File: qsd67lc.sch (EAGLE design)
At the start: 43 parts, among them IC1 MEGA8-P, IC2 BTS555E3146, IC3 MAX3232CPE, IC4 LM2576S, T1 BCR141, U1 HC_05, X2 RS232

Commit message: added connectors fixed rs232 dsub9 pinning added current supply circuit
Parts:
- added R10, R11, R13: 10k, rcl:R-EU_R0805
- added X1: FFKV3, con-phoenix-508:FFKV3
- added X3, X4: FFKV4, con-phoenix-508:FFKV4
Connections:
- removed net IGN_OUT: IC2.O1, IC2.O2
- new net 12V_OUT: IC2.O1, IC2.O2, X4-4.2
- new net IGN0_IN: R13.2, X3-1.2
- new net IGN0_OUT: X4-1.2
- new net IGN1_IN: X3-2.2
- new net IGN1_OUT: X4-2.2
- new net IGN2_IN: X3-3.2
- new net IGN2_OUT: X4-3.2
- new net QS+: IC1.PD2(INT0), R10.1, X1-2.2
- new net QS-: X1-1.2
- net +12V: now also X3-4.2
- net +3V3: now also R10.2
- net GND: now also R11.1, X1-3.2
- net RPM_INT: now also R11.2, R13.1
- net RS232_RX: now also X2.3; no longer X2.2
- net RS232_TX: now also X2.2; no longer X2.3

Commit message: added correct connector devices
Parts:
- removed X1: FFKV3, con-phoenix-508:FFKV3
- removed X3, X4: FFKV4, con-phoenix-508:FFKV4
- added CON1, CON2: RIA-AKL-230-04, con-ria:RIA-AKL-230-04
- added CON3: RIA-AKL-230-03, con-ria:RIA-AKL-230-03
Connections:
- removed net IGN1_IN: X3-2.2
- new net ING1_IN: CON1.P$2
- net +12V: now also CON1.P$4; no longer X3-4.2
- net 12V_OUT: now also CON2.P$4; no longer X4-4.2
- net GND: now also CON3.P$1; no longer X1-3.2
- net IGN0_IN: now also CON1.P$3; no longer X3-1.2
- net IGN0_OUT: now also CON2.P$3; no longer X4-1.2
- net IGN1_OUT: now also CON2.P$2; no longer X4-2.2
- net IGN2_IN: now also CON1.P$1; no longer X3-3.2
- net IGN2_OUT: now also CON2.P$1; no longer X4-3.2
- net QS+: now also CON3.P$3; no longer X1-2.2
- net QS-: now also CON3.P$2; no longer X1-1.2
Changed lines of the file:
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@@
 <part name="+3V6" library="supply1" library_urn="urn:adsk.eagle:library:371" deviceset="+3V3" device=""/>
 <part name="R10" library="rcl" library_urn="urn:adsk.eagle:library:334" deviceset="R-EU_" device="R0805" package3d_urn="urn:adsk.eagle:package:23553/2" value="10k"/>
-<part name="X1" library="con-phoenix-508" library_urn="urn:adsk.eagle:library:176" deviceset="FFKV3" device="" package3d_urn="urn:adsk.eagle:package:9576/1"/>
-<part name="X3" library="con-phoenix-508" library_urn="urn:adsk.eagle:library:176" deviceset="FFKV4" device="" package3d_urn="urn:adsk.eagle:package:9586/1"/>
-<part name="X4" library="con-phoenix-508" library_urn="urn:adsk.eagle:library:176" deviceset="FFKV4" device="" package3d_urn="urn:adsk.eagle:package:9586/1"/>
 <part name="R11" library="rcl" library_urn="urn:adsk.eagle:library:334" deviceset="R-EU_" device="R0805" package3d_urn="urn:adsk.eagle:package:23553/2" value="10k"/>
 <part name="R13" library="rcl" library_urn="urn:adsk.eagle:library:334" deviceset="R-EU_" device="R0805" package3d_urn="urn:adsk.eagle:package:23553/2" value="10k"/>
 <part name="GND9" library="supply1" library_urn="urn:adsk.eagle:library:371" deviceset="GND" device=""/>
+<part name="CON1" library="con-ria" deviceset="RIA-AKL-230-04" device=""/>
+<part name="CON2" library="con-ria" deviceset="RIA-AKL-230-04" device=""/>
+<part name="CON3" library="con-ria" deviceset="RIA-AKL-230-03" device=""/>
+<part name="GND17" library="supply1" library_urn="urn:adsk.eagle:library:371" deviceset="GND" device=""/>
+<part name="P+4" library="supply1" library_urn="urn:adsk.eagle:library:371" deviceset="+12V" device=""/>
 </parts>
 <sheets>
@@
 </plain>
 <instances>
-<instance part="X1" gate="-1" x="-7.62" y="-35.56" rot="R180">
-<attribute name="NAME" x="-7.366" y="-36.449" size="1.778" layer="95"/>
-</instance>
-<instance part="X1" gate="-2" x="-7.62" y="-30.48" rot="R180">
-<attribute name="NAME" x="-7.366" y="-31.369" size="1.778" layer="95"/>
-<attribute name="VALUE" x="-5.08" y="-26.797" size="1.778" layer="96" rot="R180"/>
-</instance>
-<instance part="X3" gate="-1" x="-7.62" y="-12.7" rot="R180">
-<attribute name="NAME" x="-7.366" y="-13.589" size="1.778" layer="95"/>
-</instance>
-<instance part="X3" gate="-2" x="-7.62" y="-7.62" rot="R180">
-<attribute name="NAME" x="-7.366" y="-8.509" size="1.778" layer="95"/>
-</instance>
-<instance part="X3" gate="-3" x="-7.62" y="-2.54" rot="R180">
-<attribute name="NAME" x="-7.366" y="-3.429" size="1.778" layer="95"/>
-</instance>
-<instance part="X3" gate="-4" x="-7.62" y="2.54" rot="R180">
-<attribute name="NAME" x="-7.366" y="1.651" size="1.778" layer="95"/>
-<attribute name="VALUE" x="-5.08" y="6.223" size="1.778" layer="96" rot="R180"/>
-</instance>
-<instance part="X4" gate="-1" x="-7.62" y="12.7" rot="R180">
-<attribute name="NAME" x="-7.366" y="11.811" size="1.778" layer="95"/>
-</instance>
-<instance part="X4" gate="-2" x="-7.62" y="17.78" rot="R180">
-<attribute name="NAME" x="-7.366" y="16.891" size="1.778" layer="95"/>
-</instance>
-<instance part="X4" gate="-3" x="-7.62" y="22.86" rot="R180">
-<attribute name="NAME" x="-7.366" y="21.971" size="1.778" layer="95"/>
-</instance>
-<instance part="X4" gate="-4" x="-7.62" y="27.94" rot="R180">
-<attribute name="NAME" x="-7.366" y="27.051" size="1.778" layer="95"/>
-<attribute name="VALUE" x="-5.08" y="31.623" size="1.778" layer="96" rot="R180"/>
-</instance>
-<instance part="X1" gate="-3" x="-7.62" y="-25.4" rot="R180">
-<attribute name="NAME" x="-7.366" y="-26.289" size="1.778" layer="95"/>
-<attribute name="VALUE" x="-5.08" y="-21.717" size="1.778" layer="96" rot="R180"/>
+<instance part="CON1" gate="G$1" x="7.62" y="17.78" rot="R180"/>
+<instance part="CON2" gate="G$1" x="7.62" y="-5.08" rot="R180"/>
+<instance part="CON3" gate="G$1" x="7.62" y="-30.48" rot="R180"/>
+<instance part="GND17" gate="1" x="-33.02" y="-38.1">
+<attribute name="VALUE" x="-35.56" y="-40.64" size="1.778" layer="96"/>
+</instance>
+<instance part="P+4" gate="1" x="-33.02" y="25.4">
+<attribute name="VALUE" x="-35.56" y="20.32" size="1.778" layer="96" rot="R90"/>
 </instance>
 </instances>
@@
 </busses>
 <nets>
+<net name="+12V" class="0">
+<segment>
+<pinref part="CON1" gate="G$1" pin="P$4"/>
+<wire x1="-5.08" y1="20.32" x2="-33.02" y2="20.32" width="0.1524" layer="91"/>
+<pinref part="P+4" gate="1" pin="+12V"/>
+<wire x1="-33.02" y1="20.32" x2="-33.02" y2="22.86" width="0.1524" layer="91"/>
+</segment>
+</net>
+<net name="IGN0_IN" class="0">
+<segment>
+<pinref part="CON1" gate="G$1" pin="P$3"/>
+<wire x1="-5.08" y1="17.78" x2="-30.48" y2="17.78" width="0.1524" layer="91"/>
+<label x="-30.48" y="17.78" size="1.778" layer="95"/>
+</segment>
+</net>
+<net name="ING1_IN" class="0">
+<segment>
+<pinref part="CON1" gate="G$1" pin="P$2"/>
+<wire x1="-5.08" y1="15.24" x2="-30.48" y2="15.24" width="0.1524" layer="91"/>
+<label x="-30.48" y="15.24" size="1.778" layer="95"/>
+</segment>
+</net>
+<net name="IGN2_IN" class="0">
+<segment>
+<pinref part="CON1" gate="G$1" pin="P$1"/>
+<wire x1="-5.08" y1="12.7" x2="-30.48" y2="12.7" width="0.1524" layer="91"/>
+<label x="-30.48" y="12.7" size="1.778" layer="95"/>
+</segment>
+</net>
+<net name="12V_OUT" class="0">
+<segment>
+<pinref part="CON2" gate="G$1" pin="P$4"/>
+<wire x1="-5.08" y1="-2.54" x2="-30.48" y2="-2.54" width="0.1524" layer="91"/>
+<label x="-30.48" y="-2.54" size="1.778" layer="95"/>
+</segment>
+</net>
+<net name="IGN0_OUT" class="0">
+<segment>
+<pinref part="CON2" gate="G$1" pin="P$3"/>
+<wire x1="-5.08" y1="-5.08" x2="-30.48" y2="-5.08" width="0.1524" layer="91"/>
+<label x="-30.48" y="-5.08" size="1.778" layer="95"/>
+</segment>
+</net>
+<net name="IGN1_OUT" class="0">
+<segment>
+<pinref part="CON2" gate="G$1" pin="P$2"/>
+<wire x1="-5.08" y1="-7.62" x2="-30.48" y2="-7.62" width="0.1524" layer="91"/>
+<label x="-30.48" y="-7.62" size="1.778" layer="95"/>
+</segment>
+</net>
+<net name="IGN2_OUT" class="0">
+<segment>
+<pinref part="CON2" gate="G$1" pin="P$1"/>
+<wire x1="-5.08" y1="-10.16" x2="-30.48" y2="-10.16" width="0.1524" layer="91"/>
+<label x="-30.48" y="-10.16" size="1.778" layer="95"/>
+</segment>
+</net>
 <net name="QS+" class="0">
 <segment>
-<pinref part="X1" gate="-2" pin="2"/>
-<wire x1="-15.24" y1="-30.48" x2="-45.72" y2="-30.48" width="0.1524" layer="91"/>
-<label x="-45.72" y="-30.48" size="1.778" layer="95"/>
+<pinref part="CON3" gate="G$1" pin="P$3"/>
+<wire x1="-5.08" y1="-27.94" x2="-30.48" y2="-27.94" width="0.1524" layer="91"/>
+<label x="-30.48" y="-27.94" size="1.778" layer="95"/>
 </segment>
 </net>
 <net name="QS-" class="0">
 <segment>
-<pinref part="X1" gate="-1" pin="2"/>
-<wire x1="-15.24" y1="-35.56" x2="-45.72" y2="-35.56" width="0.1524" layer="91"/>
-<label x="-45.72" y="-35.56" size="1.778" layer="95"/>
-</segment>
-</net>
-<net name="12V_OUT" class="0">
-<segment>
-<pinref part="X4" gate="-4" pin="2"/>
-<wire x1="-15.24" y1="27.94" x2="-45.72" y2="27.94" width="0.1524" layer="91"/>
-<label x="-45.72" y="27.94" size="1.778" layer="95"/>
-</segment>
-</net>
-<net name="IGN2_OUT" class="0">
-<segment>
-<pinref part="X4" gate="-3" pin="2"/>
-<wire x1="-15.24" y1="22.86" x2="-45.72" y2="22.86" width="0.1524" layer="91"/>
-<label x="-45.72" y="22.86" size="1.778" layer="95"/>
-</segment>
-</net>
-<net name="IGN1_OUT" class="0">
-<segment>
-<pinref part="X4" gate="-2" pin="2"/>
-<wire x1="-15.24" y1="17.78" x2="-45.72" y2="17.78" width="0.1524" layer="91"/>
-<label x="-45.72" y="17.78" size="1.778" layer="95"/>
-</segment>
-</net>
-<net name="IGN0_OUT" class="0">
-<segment>
-<pinref part="X4" gate="-1" pin="2"/>
-<wire x1="-15.24" y1="12.7" x2="-45.72" y2="12.7" width="0.1524" layer="91"/>
-<label x="-45.72" y="12.7" size="1.778" layer="95"/>
-</segment>
-</net>
-<net name="+12V" class="0">
-<segment>
-<pinref part="X3" gate="-4" pin="2"/>
-<wire x1="-15.24" y1="2.54" x2="-45.72" y2="2.54" width="0.1524" layer="91"/>
-<label x="-45.72" y="2.54" size="1.778" layer="95"/>
-</segment>
-</net>
-<net name="IGN2_IN" class="0">
-<segment>
-<pinref part="X3" gate="-3" pin="2"/>
-<wire x1="-15.24" y1="-2.54" x2="-45.72" y2="-2.54" width="0.1524" layer="91"/>
-<label x="-45.72" y="-2.54" size="1.778" layer="95"/>
-</segment>
-</net>
-<net name="IGN1_IN" class="0">
-<segment>
-<pinref part="X3" gate="-2" pin="2"/>
-<wire x1="-15.24" y1="-7.62" x2="-45.72" y2="-7.62" width="0.1524" layer="91"/>
-<label x="-45.72" y="-7.62" size="1.778" layer="95"/>
-</segment>
-</net>
-<net name="IGN0_IN" class="0">
-<segment>
-<pinref part="X3" gate="-1" pin="2"/>
-<wire x1="-15.24" y1="-12.7" x2="-45.72" y2="-12.7" width="0.1524" layer="91"/>
-<label x="-45.72" y="-12.7" size="1.778" layer="95"/>
+<pinref part="CON3" gate="G$1" pin="P$2"/>
+<wire x1="-5.08" y1="-30.48" x2="-30.48" y2="-30.48" width="0.1524" layer="91"/>
+<label x="-30.48" y="-30.48" size="1.778" layer="95"/>
 </segment>
 </net>
 <net name="GND" class="0">
 <segment>
-<pinref part="X1" gate="-3" pin="2"/>
-<wire x1="-15.24" y1="-25.4" x2="-45.72" y2="-25.4" width="0.1524" layer="91"/>
-<label x="-45.72" y="-25.4" size="1.778" layer="95"/>
-</segment>
-</net>
+<pinref part="CON3" gate="G$1" pin="P$1"/>
+<wire x1="-5.08" y1="-33.02" x2="-33.02" y2="-33.02" width="0.1524" layer="91"/>
+<pinref part="GND17" gate="1" pin="GND"/>
+<wire x1="-33.02" y1="-33.02" x2="-33.02" y2="-35.56" width="0.1524" layer="91"/>
+</segment>
+</net>

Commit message: started with the layout
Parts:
- added C11: 100n, rcl:C-EUC0805
- C5, C6, C7, C8: value (none) -> 100n; device rcl:CPOL-EUE2.5-6 -> rcl:C-EUC0805
- R11: value 10k -> 33k
- R13: value 10k -> 67k
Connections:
- removed net IGN0_OUT: CON2.P$3
- removed net IGN1_OUT: CON2.P$2
- removed net IGN2_IN: CON1.P$1
- removed net IGN2_OUT: CON2.P$1
- removed net ING1_IN: CON1.P$2
- new net IGN0: CON1.P$3, CON2.P$3
- new net IGN1: CON1.P$2, CON2.P$2
- new net IGN2: CON1.P$1, CON2.P$1
- net +3V3: now also C11.1
- net GND: now also C11.2, C5.2, C6.2; no longer C7.-, C8.+
- net IGN0_IN: no longer CON1.P$3
- net N$11: now also C5.1; no longer C7.+
- net N$15: now also C6.1; no longer C8.-
- net N$17: now also C7.2; no longer C5.+
- net N$18: now also C8.2; no longer C6.+
- net N$19: now also C8.1; no longer C6.-
- net N$20: now also C7.1; no longer C5.-
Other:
- note added: "IGN_IN"
- note added: "IGN_OUT"
- note added: "SENSOR"

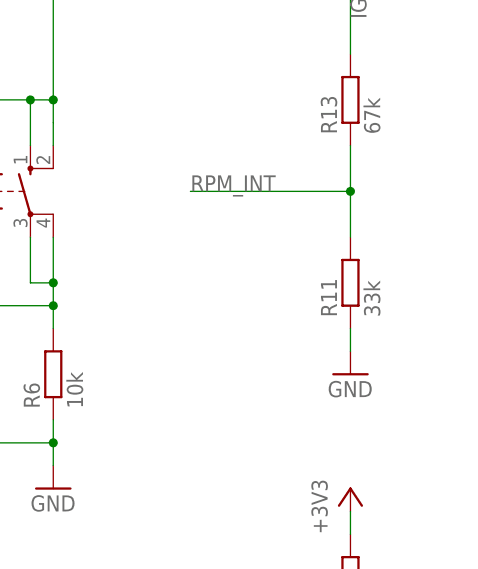
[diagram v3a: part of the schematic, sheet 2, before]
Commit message: added zener diode for overvoltage protection
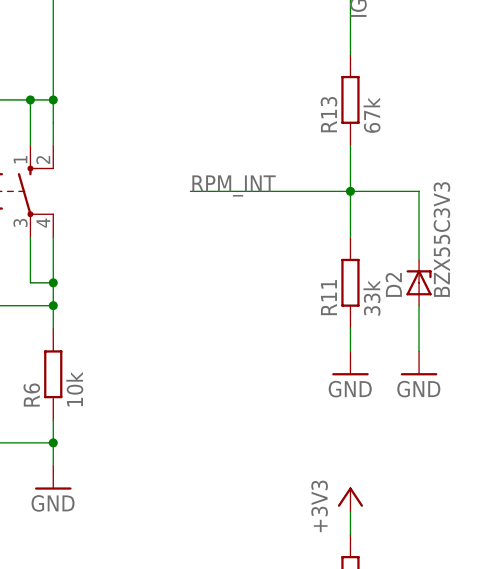
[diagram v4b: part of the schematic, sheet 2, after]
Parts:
- added D2: BZX55C3V3, diode:BZX55
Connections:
- net GND: now also D2.A
- net RPM_INT: now also D2.C
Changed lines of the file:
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@@
 <part name="C7" library="rcl" library_urn="urn:adsk.eagle:library:334" deviceset="C-EU" device="C0805" package3d_urn="urn:adsk.eagle:package:23617/2" value="100n"/>
 <part name="C8" library="rcl" library_urn="urn:adsk.eagle:library:334" deviceset="C-EU" device="C0805" package3d_urn="urn:adsk.eagle:package:23617/2" value="100n"/>
+<part name="D2" library="diode" library_urn="urn:adsk.eagle:library:210" deviceset="BZX55" device="" package3d_urn="urn:adsk.eagle:package:43342/1" value="BZX55C3V3"/>
+<part name="GND19" library="supply1" library_urn="urn:adsk.eagle:library:371" deviceset="GND" device=""/>
 </parts>
 <sheets>
@@
 <instance part="GND9" gate="1" x="162.56" y="5.08">
 <attribute name="VALUE" x="160.02" y="2.54" size="1.778" layer="96"/>
+</instance>
+<instance part="D2" gate="1" x="170.18" y="15.24" rot="R90">
+<attribute name="NAME" x="168.275" y="13.462" size="1.778" layer="95" rot="R90"/>
+<attribute name="VALUE" x="173.609" y="13.462" size="1.778" layer="96" rot="R90"/>
+</instance>
+<instance part="GND19" gate="1" x="170.18" y="5.08">
+<attribute name="VALUE" x="167.64" y="2.54" size="1.778" layer="96"/>
 </instance>
 </instances>
@@
 <wire x1="162.56" y1="10.16" x2="162.56" y2="7.62" width="0.1524" layer="91"/>
 </segment>
+<segment>
+<pinref part="GND19" gate="1" pin="GND"/>
+<pinref part="D2" gate="1" pin="A"/>
+<wire x1="170.18" y1="7.62" x2="170.18" y2="12.7" width="0.1524" layer="91"/>
+</segment>
 </net>
 <net name="RXD" class="0">
@@
 <junction x="162.56" y="25.4"/>
 <label x="144.78" y="25.4" size="1.778" layer="95"/>
-</segment>
-</net>
+<pinref part="D2" gate="1" pin="C"/>
+<wire x1="162.56" y1="25.4" x2="170.18" y2="25.4" width="0.1524" layer="91"/>
+<wire x1="170.18" y1="25.4" x2="170.18" y2="17.78" width="0.1524" layer="91"/>
+</segment>
+</net>

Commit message: added an ftdi chip to use usb directly instead of rs232 dsub connector
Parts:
- added C12: (no value), rcl:C-EUC0805
- added IC5: FT232RL, ftdichip:FT232RL
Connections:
- net +12V: now also C12.1
- net GND: now also C12.2
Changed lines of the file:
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@@
 <part name="D2" library="diode" library_urn="urn:adsk.eagle:library:210" deviceset="BZX55" device="" package3d_urn="urn:adsk.eagle:package:43342/1" value="BZX55C3V3"/>
 <part name="GND19" library="supply1" library_urn="urn:adsk.eagle:library:371" deviceset="GND" device=""/>
+<part name="C12" library="rcl" library_urn="urn:adsk.eagle:library:334" deviceset="C-EU" device="C0805" package3d_urn="urn:adsk.eagle:package:23617/2"/>
+<part name="GND20" library="supply1" library_urn="urn:adsk.eagle:library:371" deviceset="GND" device=""/>
+<part name="IC5" library="ftdichip" library_urn="urn:adsk.eagle:library:231" deviceset="FT232R" device="L" package3d_urn="urn:adsk.eagle:package:14013/1"/>
 </parts>
 <sheets>
@@
 <attribute name="VALUE" x="106.68" y="35.56" size="1.778" layer="96" rot="R90"/>
 </instance>
+<instance part="C12" gate="G$1" x="22.86" y="12.7">
+<attribute name="NAME" x="24.384" y="13.081" size="1.778" layer="95"/>
+<attribute name="VALUE" x="24.384" y="8.001" size="1.778" layer="96"/>
+</instance>
+<instance part="GND20" gate="1" x="22.86" y="-7.62">
+<attribute name="VALUE" x="20.32" y="-10.16" size="1.778" layer="96"/>
+</instance>
 </instances>
 <busses>
@@
 <pinref part="GND14" gate="1" pin="GND"/>
 <wire x1="109.22" y1="7.62" x2="109.22" y2="-5.08" width="0.1524" layer="91"/>
+</segment>
+<segment>
+<pinref part="C12" gate="G$1" pin="2"/>
+<pinref part="GND20" gate="1" pin="GND"/>
+<wire x1="22.86" y1="7.62" x2="22.86" y2="-5.08" width="0.1524" layer="91"/>
 </segment>
 </net>
@@
 <pinref part="IC4" gate="A" pin="VIN"/>
 <wire x1="15.24" y1="15.24" x2="15.24" y2="27.94" width="0.1524" layer="91"/>
-<wire x1="15.24" y1="27.94" x2="48.26" y2="27.94" width="0.1524" layer="91"/>
+<wire x1="15.24" y1="27.94" x2="22.86" y2="27.94" width="0.1524" layer="91"/>
 <pinref part="P+3" gate="1" pin="+12V"/>
+<wire x1="22.86" y1="27.94" x2="48.26" y2="27.94" width="0.1524" layer="91"/>
 <wire x1="15.24" y1="38.1" x2="15.24" y2="27.94" width="0.1524" layer="91"/>
 <junction x="15.24" y="27.94"/>
+<pinref part="C12" gate="G$1" pin="1"/>
+<wire x1="22.86" y1="15.24" x2="22.86" y2="27.94" width="0.1524" layer="91"/>
+<junction x="22.86" y="27.94"/>
 </segment>
 </net>
@@
 </nets>
 </sheet>
+<sheet>
+<description>USB FTDI</description>
+<plain>
+</plain>
+<instances>
+<instance part="IC5" gate="1" x="0" y="0">
+<attribute name="NAME" x="-10.16" y="26.67" size="1.778" layer="95"/>
+<attribute name="VALUE" x="-10.16" y="-30.48" size="1.778" layer="96"/>
+</instance>
+</instances>
+<busses>
+</busses>
+<nets>
+</nets>
+</sheet>

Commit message: working commit
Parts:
- added U2: (no value), MicroUSB:USB""
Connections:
- new net USB_D+: U2.D+
- new net USB_D-: U2.D-
